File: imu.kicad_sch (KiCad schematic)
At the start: 0 parts

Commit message: Initial component symbol placement
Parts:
- added U10: ICM-42670-P, Library:LGA-14_L3.0-W2.5-P0.50-TL_QMI8658A, symbol Library:ICM-42670-P
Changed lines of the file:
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@@
 	(generator_version "9.0")
 	(paper "A4")
+	(symbol
+		(lib_id "Library:ICM-42670-P")
+		(at 142.24 91.44 0)
+		(unit 1)
+		(exclude_from_sim no)
+		(in_bom yes)
+		(on_board yes)
+		(dnp no)
+		(fields_autoplaced yes)
+		(property "Reference" "U10"
+			(at 142.24 76.2 0)
+			(effects
+				(font
+					(size 1.27 1.27)
+				)
+			)
+		)
+		(property "Value" "ICM-42670-P"
+			(at 142.24 78.74 0)
+			(effects
+				(font
+					(size 1.27 1.27)
+				)
+			)
+		)
+		(property "Footprint" "Library:LGA-14_L3.0-W2.5-P0.50-TL_QMI8658A"
+			(at 142.24 106.68 0)
+			(effects
+				(font
+					(size 1.27 1.27)
+				)
+				(hide yes)
+			)
+		)
+		(property "Datasheet" "https://www.lcsc.com/datasheet/C3288646.pdf"
+			(at 142.24 109.22 0)
+			(effects
+				(font
+					(size 1.27 1.27)
+				)
+				(hide yes)
+			)
+		)
+		(property "Description" ""
+			(at 142.24 91.44 0)
+			(effects
+				(font
+					(size 1.27 1.27)
+				)
+				(hide yes)
+			)
+		)
+		(property "Manufacturer" "TDK InvenSense(应美盛)"
+			(at 142.24 111.76 0)
+			(effects
+				(font
+					(size 1.27 1.27)
+				)
+				(hide yes)
+			)
+		)
+		(property "MPN" "ICM-42670-P"
+			(at 142.24 114.3 0)
+			(effects
+				(font
+					(size 1.27 1.27)
+				)
+				(hide yes)
+			)
+		)
+		(property "LCSC Part" "C3288646"
+			(at 142.24 116.84 0)
+			(effects
+				(font
+					(size 1.27 1.27)
+				)
+				(hide yes)
+			)
+		)
+		(pin "1"
+		)
+		(pin "10"
+		)
+		(pin "11"
+		)
+		(pin "2"
+		)
+		(pin "12"
+		)
+		(pin "14"
+		)
+		(pin "3"
+		)
+		(pin "5"
+		)
+		(pin "7"
+		)
+		(pin "8"
+		)
+		(pin "6"
+		)
+		(pin "13"
+		)
+		(pin "9"
+		)
+		(pin "4"
+		)
+		(instances
+			(project ""
+				(path "/6af311bf-2fb1-446c-8c7e-7c930a463809/ed1a9db8-7854-467e-9082-97c89d0d2650"
+					(reference "U11")
+					(unit 1)
+				)
+				(path "/6af311bf-2fb1-446c-8c7e-7c930a463809/fbc732a7-6283-4cfb-8013-38c8e1d06b9d"
+					(reference "U10")
+					(unit 1)
+				)
+			)
+		)
+	)
 )

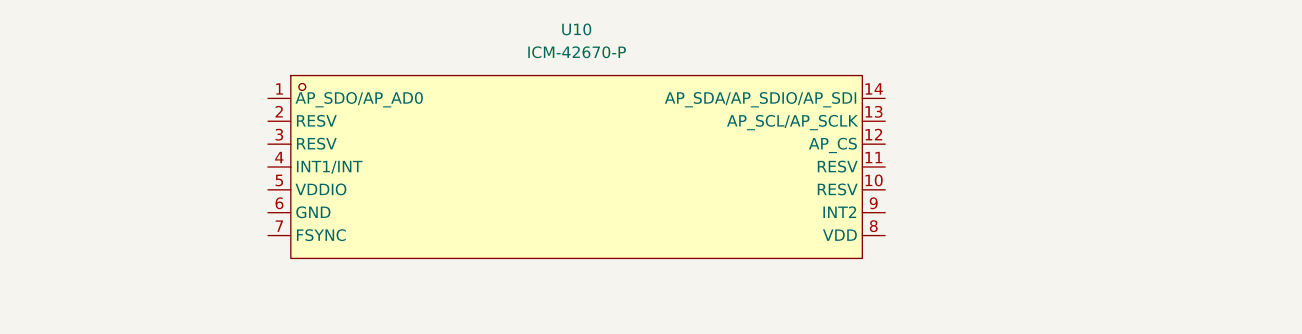
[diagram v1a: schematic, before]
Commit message: MCU implementation start Still needs component schematic checks & component integration with MCU
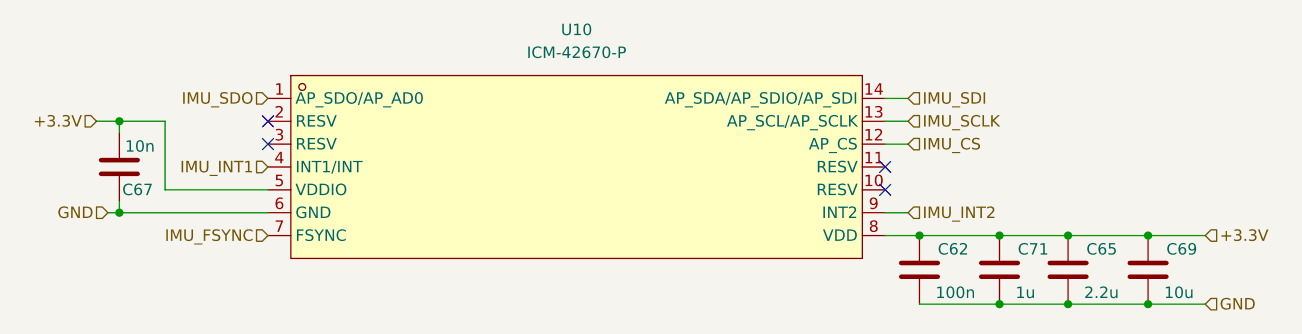
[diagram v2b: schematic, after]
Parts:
- added C62: 100n, symbol Device:C
- added C65: 2.2u, symbol Device:C
- added C67: 10n, symbol Device:C
- added C69: 10u, symbol Device:C
- added C71: 1u, symbol Device:C
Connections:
- net IMU_SDO: now reaches U10.1 (AP_SDO/AP_AD0)
- net IMU_CS: now reaches U10.12 (AP_CS)
- net IMU_SCLK: now reaches U10.13 (AP_SCL/AP_SCLK)
- net IMU_SDI: now reaches U10.14 (AP_SDA/AP_SDIO/AP_SDI)
- net IMU_INT1: now reaches U10.4 (INT1/INT)
- net +3.3V: now reaches U10.5 (VDDIO)
- net +3.3V: now also U10.8 (VDD), C62.1, C65.1, C67.1, C69.1, C71.1
- net GND: now reaches U10.6 (GND)
- net GND: now also C62.2, C65.2, C67.2, C69.2, C71.2
- net IMU_FSYNC: now reaches U10.7 (FSYNC)
- net IMU_INT2: now reaches U10.9 (INT2)
- no-connect marks 0 -> 4
